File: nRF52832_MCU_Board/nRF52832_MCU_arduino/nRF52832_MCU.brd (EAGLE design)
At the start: 45.7 x 22.9 mm, 19 parts, among them J1 TSW-116-02-S-S, J2 TSW-116-02-S-S, U1 NRF52832, X1 32MHz

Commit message: Finished? footprint and symbol for nRF5, QFN. Done som experimenting on board layouts
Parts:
- removed J1, J2: TSW-116-02-S-S, con-samtec:TSW-116-02-S-S
- added X2, X4: TSW-108-02-S-S, con-samtec:TSW-108-02-S-S
- added X3: TSW-106-02-S-S, con-samtec:TSW-106-02-S-S
- added X5: TSW-110-02-S-S, con-samtec:TSW-110-02-S-S
- U1: device nRF:QFN40P600X600X90-48N -> nRF:QFN48
- X1: device nRF:BT-XTAL_2016 -> IQD-Frequency-Products:2.0X1.6-4-PAD
- moved C13 70.6 mm to (52.1, 21.6)
- moved C11 16.1 mm to (22.9, 25.4)
- moved C2 13.8 mm to (45.7, 27.4)
- moved X1 13.7 mm to (43.1, 27.4)
- moved C6 13.7 mm to (43.8, 24.1)
- moved C10 13.7 mm to (34.5, 25.9)
- moved C5 13.7 mm to (33.7, 17.7)
- moved C7 13.7 mm to (43.8, 25.2)
- moved C8 13.7 mm to (39.8, 27.4)
- moved C9 13.7 mm to (31.4, 24.5)
- moved C1 13.7 mm to (40.9, 27.4)
- moved C3 13.7 mm to (42.5, 21.6)
- moved L1 13.7 mm to (44.5, 20.9)
- moved U1 13.7 mm to (36.8, 21.6)
- moved C4 13.6 mm to (31.4, 22.9)
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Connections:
- net GND: now also X1.2, X1.4, X5.4; no longer X1.P$2, X1.P$4
- net N$3: now also X1.3; no longer X1.P$3
- net N$4: now also X1.1; no longer X1.P$1
- net P0.00: now also X3.6; no longer J1.1
- net P0.01: now also X3.5; no longer J1.2
- net P0.02: now also X3.4; no longer J1.3
- net P0.03: now also X3.3; no longer J1.4
- net P0.04: now also X3.2; no longer J1.5
- net P0.05: now also X3.1; no longer J1.6
- net P0.06: now also X4.8; no longer J1.7
- net P0.07: now also X4.7; no longer J1.8
- net P0.08: now also X4.6; no longer J1.9
- net P0.09: now also X4.5; no longer J1.10
- net P0.10: now also X4.4; no longer J1.11
- net P0.11: now also X4.3; no longer J1.12
- net P0.12: now also X4.2; no longer J1.13
- net P0.13: now also X4.1; no longer J1.14
- net P0.14: now also X5.10; no longer J1.15
- net P0.15: now also X5.9; no longer J1.16
- net P0.16: now also X5.8; no longer J2.16
- net P0.17: now also X5.7; no longer J2.15
- net P0.18: now also X5.6; no longer J2.14
- net P0.19: now also X5.5; no longer J2.13
- net P0.20: now also X5.3; no longer J2.12
- net P0.21: now also X5.2; no longer J2.11
- net P0.22: now also X5.1; no longer J2.10
- net P0.23: no longer J2.9
- net P0.24: no longer J2.8
- net P0.25: no longer J2.7
- net P0.26: no longer J2.6
- net P0.27: no longer J2.5
- net P0.28: no longer J2.4
- net P0.29: no longer J2.3
- net P0.30: no longer J2.2
- net P0.31: no longer J2.1
- net VCC: now also X2.2, X2.4, X2.5
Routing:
- net N$3: track 2.95 -> 6.57 mm
- net GND: track 26.2 -> 23.5 mm
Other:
- board size 45.7 x 22.9 mm -> 68.6 x 53.3 mm

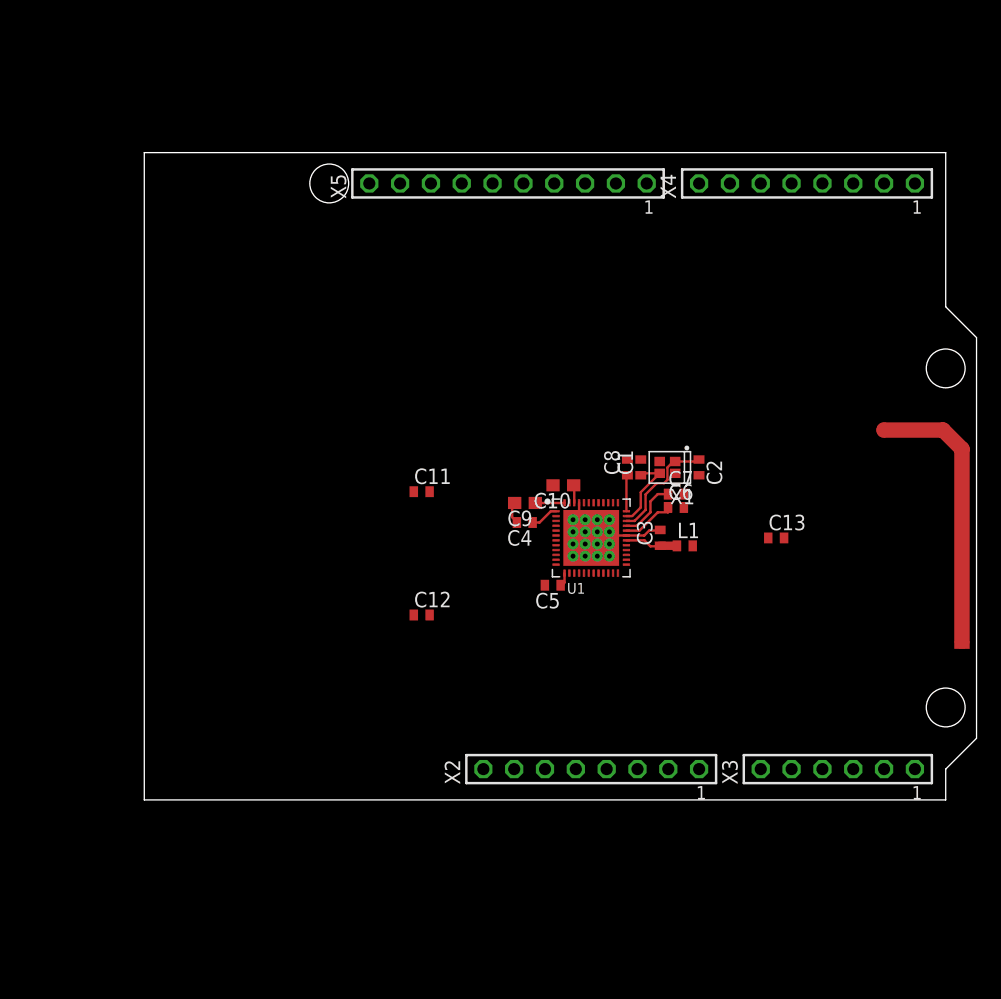
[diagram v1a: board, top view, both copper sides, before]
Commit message: Copyed layout from nano to arduino
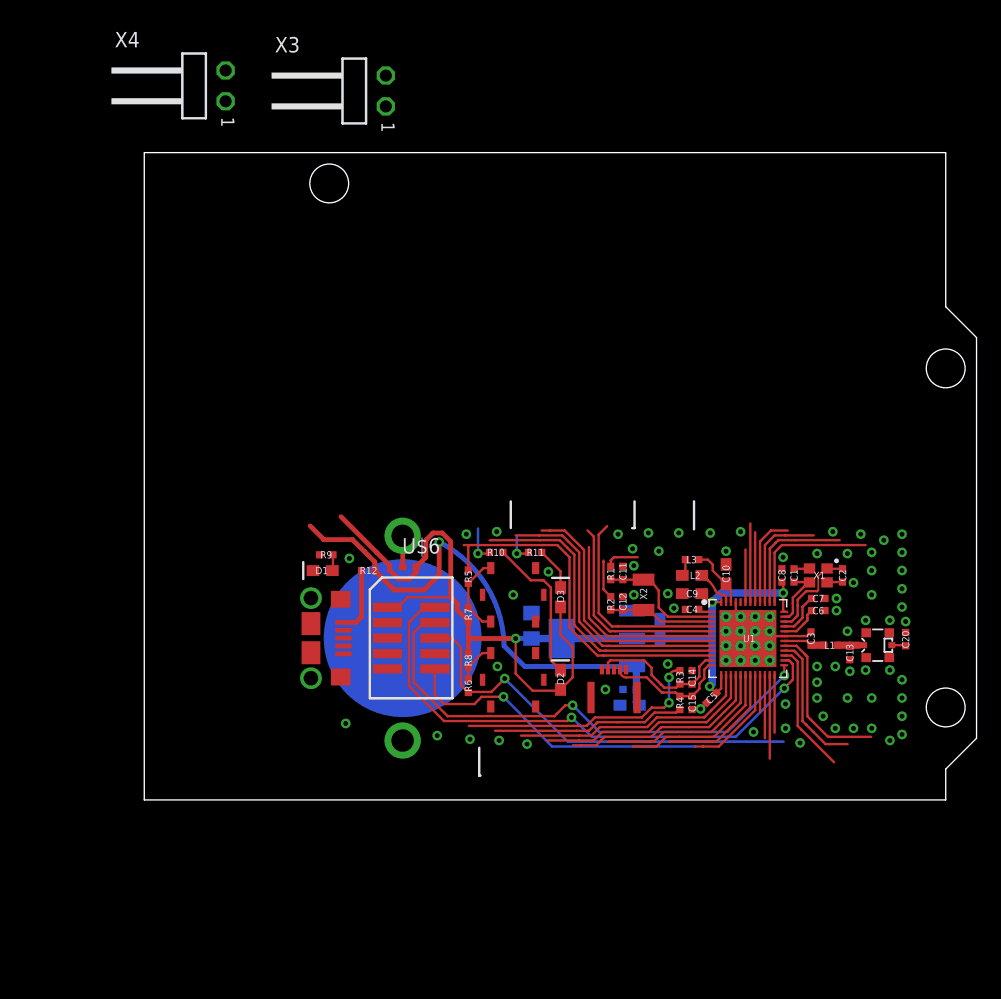
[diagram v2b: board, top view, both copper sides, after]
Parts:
- removed ANT1: 2.45GHZ_PCB_ANTENNA, nRF:PCB_ANTENNA
- removed X5: TSW-110-02-S-S, con-samtec:TSW-110-02-S-S
- added BATT1: CR1632, Nordic_misc:CR1632_HOLDER_TH
- added C14, C15: 300pF, Nordic_misc:RESC0402_N
- added C16: 100nF, Nordic_misc:RESC0402_N
- added C17, C18: 10µF, Nordic_misc:RESC0603_N
- added C19: 100µF, Nordic_misc:RESC0805_N
- added C20: TBD, Nordic_misc:RESC0402_N
- added D1, D2, D3: LED, Nordic_misc:DIOC0603_N
- added J5: MICROUSB, Nordic_misc:USB-MICRO-B-RA-SMD-PIP
- added J6: DEBUG_CONNECTOR, Nordic_misc:HDRV127P5X2-10_N
- added J7: FPC_05P-RA-SMD, Nordic_misc:FPC_05P-RA-SMD
- added J8: MM8130-2600, Nordic_misc:MM8130-2600
- added L2: 10µH, Nordic_misc:RESC0603_N
- added L3: 15nH, Nordic_misc:RESC0402_N
- added R1, R12, R2, R3, R4, U$6: 0R, Nordic_misc:RESC0402_N
- added R10, R11, R5, R6, R9: 330R, Nordic_misc:RESC0402_N
- added R7, R8: 100k, Nordic_misc:RESC0402_N
- added U$4, U$5: PANASONIC_EVQPT5A15, Nordic_misc:PANASONIC_EVQPT5A15
- added U2: TLV1117, Nordic_misc:SOT220P700-4_N
- C1, C11, C12, C2, C3, C4, C5, C6, C7, C8: device rcl:C0402 -> Nordic_misc:RESC0402_N
- C10, C9: device rcl:C0603 -> Nordic_misc:RESC0603_N
- C13: value 0.8pF -> N.C.; device rcl:C0402 -> Nordic_misc:RESC0402_N
- L1: device nRF:R0402 -> Nordic_misc:RESC0402_N
- U1: device nRF:QFN48 -> Nordic_nRF:QFN40P600X600X90-48_N
- X1: device IQD-Frequency-Products:2.0X1.6-4-PAD -> Nordic_nRF:BT-XTAL_2016_N
- X2: value TSW-108-02-S-S -> 32.768kHz; device con-samtec:TSW-108-02-S-S -> Nordic_nRF:XTAL_3215_N
- X3: value TSW-106-02-S-S -> TSW-102-02-S-S-RA; device con-samtec:TSW-106-02-S-S -> con-samtec:TSW-102-02-S-S-RA
- X4: value TSW-108-02-S-S -> TSW-102-02-S-S-RA; device con-samtec:TSW-108-02-S-S -> con-samtec:TSW-102-02-S-S-RA
- moved X3 68.0 mm to (18.4, 58.4), turned to 270 degrees
- moved X4 50.1 mm to (5.18, 58.8), turned to 270 degrees
- moved C11 17.9 mm to (39.4, 18.7), turned to 270 degrees
- moved C12 16.6 mm to (39.4, 16.2), turned to 270 degrees
- moved C5 16.0 mm to (46.7, 8.40), turned to 225 degrees
- moved C9 15.7 mm to (45.1, 17.0)
- moved C4 15.5 mm to (45.1, 15.7)
- moved C8 15.5 mm to (52.5, 18.5)
- moved C1 15.5 mm to (53.5, 18.5)
- moved U1 15.3 mm to (49.7, 13.3)
- moved X1 15.3 mm to (55.5, 18.5)
- moved C10 15.3 mm to (47.9, 18.6), turned to 90 degrees
- moved X2 15.0 mm to (41.1, 16.9), turned to 270 degrees
- moved C3 14.9 mm to (54.9, 13.3)
- moved C2 14.8 mm to (57.5, 18.5)
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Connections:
- net N$4 renamed X1
- removed net N$14: U1.26
- removed net N$15: U1.25
- removed net P0.18: U1.21, X5.6
- removed net P0.21: U1.24, X5.2
- removed net VCC: C5.1, C8.1, C9.1, U1.13, U1.36, U1.48, X2.2, X2.4, X2.5
- new net N$2: L2.2, L3.1
- new net N$4: L2.1, U1.47
- new net N$5: C13.1, J8.IN, L1.2
- new net N$6: R6.2, R8.1, U$5.1, U$5.2
- new net N$7: R5.2, R7.1, U$4.1, U$4.2
- new net N$8: D2.1, R10.2
- new net N$9: D3.1, R11.2
- new net NFC1: C14.2, J7.2, R3.1, U1.11
- new net NFC2: C15.1, J7.4, R4.2, U1.12
- new net P0.18/SWO: J6.10, U1.21
- new net P0.21/RESET: J6.6, R6.1, U1.24
- new net SWDCLK: J6.4, U1.25
- new net SWDIO: J6.2, U1.26
- new net VCC_P5V0_USB: J5.1, R12.1
- new net VDD_LED: D1.2, R9.2
- new net VDD_P3V3: C18.1, C19.1, C5.1, C8.1, C9.1, D2.2, D3.2, J6.1, R7.2, R8.2, U$6.2, U1.13, U1.36, U1.48, U2.2, U2.4
- new net VDD_P3V3_BATT: BATT1.2, BATT1.3, U$6.1
- new net VDD_P5V0: C16.1, C17.1, D1.1, R12.2, U2.3
- new net XL1: C11.2, R1.1, U1.2, X2.1
- new net XL2: C12.2, R2.2, U1.3, X2.2
- net DEC4: now also L3.2
- net GND: now also BATT1.1, C11.1, C12.1, C14.1, C15.2, C16.2, C17.2, C18.2, C19.2, C20.2, J5.5, J6.3, J6.5, J6.9, J8.1, J8.2, J8.3, J8.4, R9.1, U$4.3, U$4.4, U$4.5, U$4.6, U$5.3, U$5.4, U$5.5, U$5.6, U2.1; no longer X5.4
- net N$1: now also C20.1, J8.OUT; no longer ANT1.P$1, C13.1, L1.2
- net P0.00: now also R1.2; no longer U1.2, X3.6
- net P0.01: now also R2.1; no longer U1.3, X3.5
- net P0.02: no longer X3.4
- net P0.03: no longer X3.3
- net P0.04: no longer X3.2
- net P0.05: no longer X3.1
- net P0.06: now also R11.1; no longer X4.8
- net P0.07: now also R10.1; no longer X4.7
- net P0.08: now also R5.1; no longer X4.6
- net P0.09: now also R3.2; no longer U1.11, X4.5
- net P0.10: now also R4.1; no longer U1.12, X4.4
- net P0.11: no longer X4.3
- net P0.12: no longer X4.2
- net P0.13: no longer X4.1
- net P0.14: no longer X5.10
- net P0.15: no longer X5.9
- net P0.16: no longer X5.8
- net P0.17: no longer X5.7
- net P0.19: no longer X5.5
- net P0.20: no longer X5.3
- net P0.22: no longer X5.1
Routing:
- net VDD_P3V3: track 0.00 -> 89.3 mm, vias 0 -> 4
- net SWDIO: track 0.00 -> 45.5 mm, vias 0 -> 2
- net SWDCLK: track 0.00 -> 41.9 mm, vias 0 -> 2
- net VDD_P5V0: track 0.00 -> 41.6 mm, vias 0 -> 1
- net P0.21/RESET: track 0.00 -> 39.9 mm, vias 0 -> 1
- net P0.08: track 0.00 -> 29.6 mm
- net P0.18/SWO: track 0.00 -> 29.0 mm, vias 0 -> 1
- net P0.07: track 0.00 -> 28.5 mm, vias 0 -> 1
- net P0.06: track 0.00 -> 25.7 mm, vias 0 -> 1
- net P0.05: track 0.00 -> 21.2 mm
- net P0.09: track 0.00 -> 20.5 mm, vias 0 -> 2
- net P0.11: track 0.00 -> 20.0 mm
- net P0.12: track 0.00 -> 18.5 mm
- net P0.03: track 0.00 -> 17.5 mm
- net P0.02: track 0.00 -> 17.2 mm
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
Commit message: Looked at arduino layout
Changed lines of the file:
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@@
 <plain>
 <rectangle x1="53.14" y1="11.5" x2="56.74" y2="15.3" layer="41"/>
-<wire x1="27.7" y1="2" x2="27.6" y2="2" width="0.2" layer="21"/>
-<wire x1="27.6" y1="2" x2="27.6" y2="4.3" width="0.2" layer="21"/>
-<wire x1="40.2" y1="22.4" x2="40.4" y2="22.4" width="0.2" layer="21"/>
-<wire x1="40.4" y1="22.4" x2="40.4" y2="24.6" width="0.2" layer="21"/>
-<wire x1="45.3" y1="24.6" x2="45.3" y2="22.3" width="0.2" layer="21"/>
-<wire x1="30.2" y1="24.6" x2="30.2" y2="22.4" width="0.2" layer="21"/>
 <wire x1="0" y1="0" x2="66.04" y2="0" width="0" layer="20"/>
 <wire x1="66.04" y1="53.34" x2="0" y2="53.34" width="0" layer="20"/>
